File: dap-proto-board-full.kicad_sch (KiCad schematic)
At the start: 71 parts, among them J1 SFV18R-1STE1HLF, J2 UJ20-C-H-G-SMT-1-P16-TR, J3 SJ-3523-SMT, J4 JST_SH_SM03B-SRSS-TB, J6 Conn_01x06, J7 Conn_01x08, SW1 B3U-1000P, U1 TPD1E05U06DPY, U2 TAD5212, U3 TXS0108ERGYR, U4 W25Q64JWUUIQ, U5 TXS0108ERGYR, U6 MSD-11-A, U7 APS6404L-SQRH-ZR, U8 RP2350A, Y1 SIT8021AI-J4-XXS-12.288E, Y2 SIT8021AI-J4-XXS-11.289E, Y3 ABM8-272-T3

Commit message: I forgort what I did
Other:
- note added: "PIO_I2C"
- note removed: "I2C_1"
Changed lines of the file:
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@@
 		)
 	)
-	(text "I2C_1"
+	(text "PIO_I2C"
 		(exclude_from_sim no)
-		(at 345.694 133.604 0)
+		(at 347.218 133.604 0)
 		(effects
 			(font

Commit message: mostly finished; just need to breakout extra gpio
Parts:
- removed C10, C6, C7: 100nF, Capacitor_SMD:C_0402_1005Metric, symbol Device:C_Small
- removed C17: 1uF, Capacitor_SMD:C_0402_1005Metric, symbol Device:C
- removed C18, C26: 10nF, Capacitor_SMD:C_0402_1005Metric, symbol Device:C_Small
- removed C19, C20, C21, C22, C23, C24, C25, C27, C28, C29, C32, C34, C9: 100nF, Capacitor_SMD:C_0402_1005Metric, symbol Device:C
- removed C33: 4.7uF, Capacitor_SMD:C_0402_1005Metric, symbol Device:C
- removed C36: 2.2uF, Capacitor_SMD:C_0402_1005Metric, symbol Device:C_Small
- removed C5: 13pF, Capacitor_SMD:C_0402_1005Metric, symbol Device:C_Small
- removed J4: JST_SH_SM03B-SRSS-TB, Connector_JST:JST_SH_SM03B-SRSS-TB_1x03-1MP_P1.00mm_Horizontal, symbol Connector_Generic_MountingPin:Conn_01x03_MountingPin
- removed J6: Conn_01x06, Connector_PinSocket_2.54mm:PinSocket_1x06_P2.54mm_Vertical, symbol Connector_Generic:Conn_01x06
- removed J7: Conn_01x08, Connector_PinSocket_2.54mm:PinSocket_1x08_P2.54mm_Vertical, symbol Connector_Generic:Conn_01x08
- removed R1: 100k, Resistor_SMD:R_0402_1005Metric, symbol Device:R_Small
- removed R14: 4.7k, Resistor_SMD:R_0402_1005Metric, symbol Device:R_Small
- removed R15: 10, Resistor_SMD:R_0402_1005Metric, symbol Device:R_Small
- removed R3: 10k, Resistor_SMD:R_0402_1005Metric, symbol Device:R_Small
- removed R7: 1k, Resistor_SMD:R_0402_1005Metric, symbol Device:R
- removed R8, R9: 27, Resistor_SMD:R_0402_1005Metric, symbol Device:R
- removed U1: TPD1E05U06DPY, Package_SON:Texas_DPY0002A_0.6x1mm_P0.65mm, symbol Power_Protection:TPD1E05U06DPY
- removed U3, U5: TXS0108ERGYR, Package_DFN_QFN:Texas_RGY_R-PVQFN-N20_EP2.05x3.05mm_ThermalVias, symbol Logic_LevelTranslator:TXS0108EPW
- removed U4: W25Q64JWUUIQ, Package_SON:Winbond_USON-8-1EP_3x2mm_P0.5mm_EP0.2x1.6mm, symbol Memory_Flash:W25Q128JVS
- removed U7: APS6404L-SQRH-ZR, Package_SON:Winbond_USON-8-1EP_3x2mm_P0.5mm_EP0.2x1.6mm, symbol APS6404L-3SQR-ZR:APS6404L-3SQR-ZR
- removed U8: RP2350A, Package_DFN_QFN:QFN-60-1EP_7x7mm_P0.4mm_EP3.4x3.4mm, symbol MCU_RaspberryPi:RP2350A
- removed Y1: SIT8021AI-J4-XXS-12.288E, SIT8021AI-J4-XXS-24.000000E:OSC_SIT8021AI-J4-XXS-24.000000E, symbol SIT8021AI-J4-XXS-24.000000E:SIT8021AI-J4-XXS-24.000000E
- removed Y2: SIT8021AI-J4-XXS-11.289E, SIT8021AI-J4-XXS-24.000000E:OSC_SIT8021AI-J4-XXS-24.000000E, symbol SIT8021AI-J4-XXS-24.000000E:SIT8021AI-J4-XXS-24.000000E
- added C12, C15, C21, C23: 1uF, Capacitor_SMD:C_0603_1608Metric, symbol Device:C_Small
- added C13: 22uF, Capacitor_SMD:C_0603_1608Metric, symbol Device:C_Small
- added C14: 10nF, Capacitor_SMD:C_0603_1608Metric, symbol Device:C_Small
- added C16, C20, C22: 100nF, Capacitor_SMD:C_0603_1608Metric, symbol Device:C_Small
- added R13: 47k, Resistor_SMD:R_0603_1608Metric, symbol Device:R_Small
- added R7, R8, R9: 10k, Resistor_SMD:R_0603_1608Metric, symbol Device:R_Small
- added SW2: SW_Push, Button_Switch_SMD:SW_Push_1P1T_NO_Vertical_Wuerth_434133025816, symbol Switch:SW_Push
- added U2: USBLC6-2SC6, Package_TO_SOT_SMD:SOT-23-6, symbol Power_Protection:USBLC6-2SC6
- added U4: ESP32-S3, Package_DFN_QFN:QFN-56-1EP_7x7mm_P0.4mm_EP4x4mm_ThermalVias, symbol MCU_Espressif:ESP32-S3
- C1, C11, C2, C3, C4: footprint Capacitor_SMD:C_0402_1005Metric -> Capacitor_SMD:C_0603_1608Metric
- C10: renamed from C14; footprint Capacitor_SMD:C_0402_1005Metric -> Capacitor_SMD:C_0603_1608Metric
- C17: renamed from C30; value 15pF -> 18pF; footprint Capacitor_SMD:C_0402_1005Metric -> Capacitor_SMD:C_0603_1608Metric
- C18: renamed from C31; value 15pF -> 18pF; footprint Capacitor_SMD:C_0402_1005Metric -> Capacitor_SMD:C_0603_1608Metric
- C24: renamed from C35; footprint Capacitor_SMD:C_0402_1005Metric -> Capacitor_SMD:C_0603_1608Metric
- C5: renamed from C15; footprint Capacitor_SMD:C_0402_1005Metric -> Capacitor_SMD:C_0603_1608Metric
- C6: renamed from C16; footprint Capacitor_SMD:C_0402_1005Metric -> Capacitor_SMD:C_0603_1608Metric
- C7: renamed from C8; footprint Capacitor_SMD:C_0402_1005Metric -> Capacitor_SMD:C_0603_1608Metric
- C8: renamed from C12; footprint Capacitor_SMD:C_0402_1005Metric -> Capacitor_SMD:C_0603_1608Metric
- C9: renamed from C13; footprint Capacitor_SMD:C_0402_1005Metric -> Capacitor_SMD:C_0603_1608Metric
- R1: renamed from R13; value 1k -> 0; footprint Resistor_SMD:R_0402_1005Metric -> Resistor_SMD:R_0603_1608Metric
- R10, R11, R12: value 4.7k -> 47k; footprint Resistor_SMD:R_0402_1005Metric -> Resistor_SMD:R_0603_1608Metric
- R2: value 100k -> 10k; footprint Resistor_SMD:R_0402_1005Metric -> Resistor_SMD:R_0603_1608Metric
- R4: value 10k -> 2.2; footprint Resistor_SMD:R_0402_1005Metric -> Resistor_SMD:R_0603_1608Metric
- R5, R6: footprint Resistor_SMD:R_0402_1005Metric -> Resistor_SMD:R_0603_1608Metric
- SW1: value B3U-1000P -> SW_Push; footprint Button_Switch_SMD:SW_SPST_B3U-1000P -> Button_Switch_SMD:SW_Push_1P1T_NO_Vertical_Wuerth_434133025816; LCSC PN C231329 -> (none)
- U3: renamed from U2; footprint Package_DFN_QFN:TAD5212 -> footprints:VQFN24_RGE_CORNERPADS_TEX
- Y1: renamed from Y3; value ABM8-272-T3 -> ABM8-40.000MHZ-12-B1U-T
- renumbered H2 to H1, H1 to H2, U6 to U1
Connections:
- net 3v_SD_CS is gone; now on net SD_CS: U1.2 (CS)
- net 3v_SD_DAT1 is gone; now on net SD_DAT1: U1.8 (DAT1)
- net 3v_SD_DAT2 is gone; now on net SD_DAT2: U1.1 (DAT2)
- net 3v_SD_DIN is gone; now on net SD_DIN: U1.3 (DATA_IN)
- net 3v_SD_DOUT is gone; now on net SD_DOUT: U1.7 (DATA_OUT)
- net 3v_SD_SCLK is gone; now on net SD_SCLK: U1.5 (SCLK)
- net DISP_IO_ON is gone; now on net +3V3: R2.1
- net DIS_CLK1 is gone; now on net SD_DAT2: R5.2
- net DIS_CLK2 is gone; now on net SD_CS: R6.2
- net +3V3: now also C1.2, C2.1, C24.1, R10.1, R11.1, R12.1, R4.1, R5.1, R6.1, U3.6 (IOVDD), C12.1, C13.1, C14.1, C15.1, C16.1, C20.1, C21.1, C22.1, R13.1, R7.1, R8.1, R9.1, U4.2 (VDD3P3), U4.20 (VDD3P3_RTC), U4.29 (VDD_SPI), U4.3 (VDD3P3), U4.46 (VDD3P3_CPU), U4.55 (VDDA), U4.56 (VDDA)
- net BCLK: now also U4.12 (GPIO7)
- net DIN: now also U4.9 (GPIO4)
- net FSYNC: now also U4.11 (GPIO6)
- net GND: now also C12.2, C13.2, C14.2, C15.2, C16.2, C20.2, C21.2, C22.2, C23.2, SW2.2, U2.2 (GND), U4.57 (GND); no longer R2.2
- net GPIO9: now also U4.14 (GPIO9)
- net SD_CS: now also U4.47 (MTDI)
- net SD_DAT1: now also R9.2
- net SD_DIN: now also R7.2, U4.45 (MTDO)
- net SD_DOUT: now also R8.2, U4.43 (GPIO38)
- net SD_ON: now also U4.48 (MTMS)
- net SD_SCLK: now also U4.44 (MTCK)
- net USB_D+: now also U2.4 (I/O2), U4.26 (GPIO20/USB_D+); no longer J2.A6 (D+), J2.B6 (D+)
- net USB_D-: now also U2.6 (I/O1), U4.25 (GPIO19/USB_D-); no longer J2.A7 (D-), J2.B7 (D-)
- net VBUS: now also U2.5 (VBUS)
- net XIN: now also R1.1, U4.53 (XTAL_N); no longer C17.1, Y1.1
- net XOUT: now also C17.1, Y1.1, U4.54 (XTAL_P); no longer R1.1
- net disp_LITE: now also U4.27 (GPIO21)
- net disp_MISO: now also U4.40 (GPIO35)
- net disp_MOSI: now also U4.39 (GPIO34)
- net npm_SCL: now also R10.2, U4.15 (GPIO10); no longer R11.2
- net npm_SDA: now also R11.2, U4.16 (GPIO11); no longer R10.2
- net tad_SCL: now also R13.2, U4.7 (GPIO2)
- net tad_SDA: now also U4.6 (GPIO1)
- net tad_GPO1: now reaches U3.11 (GPO1)
- net DOUT: now reaches U3.4 (DOUT)
- net DOUT: now also U4.10 (GPIO5)
- removed net +1V8: C1.2, C10.2, C2.1, C24.1, C9.2, R10.1, R11.1, R12.1, R4.1, R5.1, R6.1, U3.23 (AVDD), U3.6 (IOVDD)
- net PSRAM_CS: no longer names the net of R4.2
- net PSRAM_CS: now also C10.2, C9.2, U3.23 (AVDD)
- net disp_CS_SCL renamed disp_CS
- net disp_CS: now also U4.42 (GPIO37); no longer J1.13 (Pin_13)
- net disp_DC_SDA renamed disp_DC
- net disp_DC: now also U4.41 (GPIO36); no longer J1.14 (Pin_14)
- net disp_SCK renamed disp_SCLK
- net disp_SCLK: now also U4.38 (GPIO33)
- net ~{USB_BOOT}: no longer names the net of SW1.2
- net ~{USB_BOOT}: now also U4.5 (GPIO0)
- new net: C23.1, R2.2, SW2.1, U4.4 (CHIP_PU)
- new net: J2.A6 (D+), J2.B6 (D+), U2.3 (I/O2)
- new net: J2.A7 (D-), J2.B7 (D-), U2.1 (I/O1)
- new net GPIO13: U4.18 (GPIO13)
- new net GPIO14: U4.19 (GPIO14)
- new net GPIO15: U4.21 (XTAL_32K_P)
- new net GPIO16: U4.22 (XTAL_32K_N)
- new net GPIO17: U4.23 (GPIO17)
- new net GPIO18: U4.24 (GPIO18)
- new net GPIO43: U4.49 (U0TXD)
- new net GPIO44: U4.50 (U0RXD)
- new net GPIO45: U4.51 (GPIO45)
- new net GPIO46: U4.52 (GPIO46)
- new net GPIO8: U4.13 (GPIO8)
- new net disp_SCL: J1.13 (Pin_13)
- new net disp_SDA: J1.14 (Pin_14)
- new net npm_GPIO1: U4.17 (GPIO12)
- no-connect marks 25 -> 24
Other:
- note added: "40MHz Crystal"
- note removed: "1.8v -> 3.3v Display logic level shifter"
- note removed: "1.8v -> 3.3v SD logic level shifter"
- note removed: "12MHz Crystal"
- note removed: "Default standby"
- note removed: "Extra GPIO"
- note removed: "Flash"
- note removed: "Has internal pull ups to ensure data lines are well-defined"
- note removed: "I2C_0"
- note removed: "JST Debug Connector"
- note removed: "Make sure these resistors are close to MCU"
- note removed: "PIO_I2C"
- note removed: "PSRAM"
- note removed: "RP2350A"
- note removed: "VREG filter"
- note removed: "from load switch"
- moved on the sheet: C17, C18, C5, C6, H1, H2, J3, R1, U1, Y1

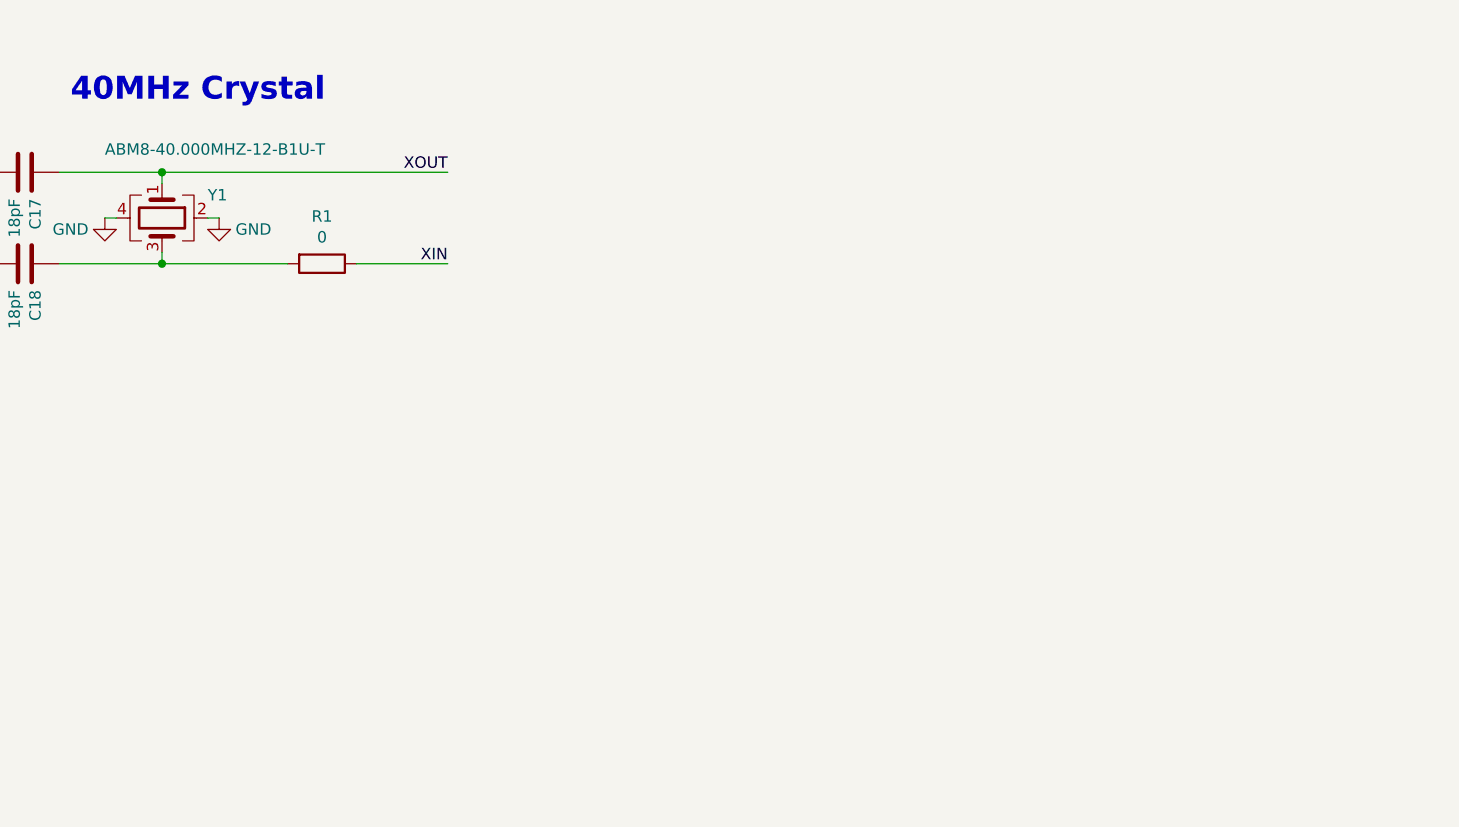
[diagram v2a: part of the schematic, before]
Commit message: breakout extra gpios; gen gerbers and images
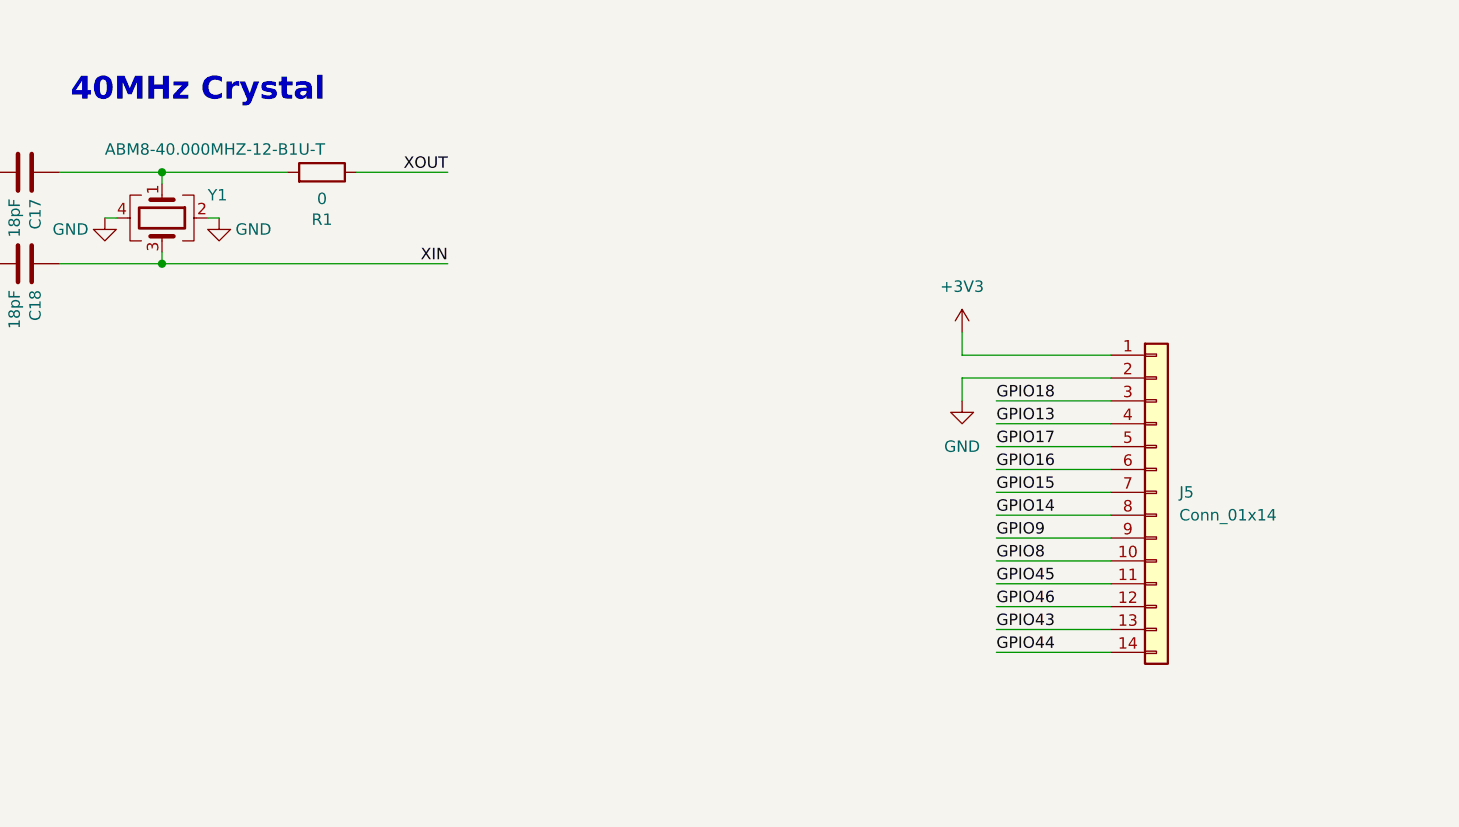
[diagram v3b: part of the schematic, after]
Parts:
- added J5: Conn_01x14, Connector_PinSocket_2.54mm:PinSocket_1x14_P2.54mm_Vertical, symbol Connector_Generic:Conn_01x14
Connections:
- net +3V3: now also J5.1 (Pin_1)
- net GND: now also J5.2 (Pin_2)
- net GPIO13: now also J5.4 (Pin_4)
- net GPIO14: now also J5.8 (Pin_8)
- net GPIO15: now also J5.7 (Pin_7)
- net GPIO16: now also J5.6 (Pin_6)
- net GPIO17: now also J5.5 (Pin_5)
- net GPIO18: now also J5.3 (Pin_3)
- net GPIO43: now also J5.13 (Pin_13)
- net GPIO44: now also J5.14 (Pin_14)
- net GPIO45: now also J5.11 (Pin_11)
- net GPIO46: now also J5.12 (Pin_12)
- net GPIO8: now also J5.10 (Pin_10)
- net GPIO9: now also J5.9 (Pin_9)
- net XIN: now also C18.1, Y1.3; no longer R1.1
- net XOUT: now also R1.1; no longer C17.1, Y1.1
- new net: C17.1, R1.2, Y1.1
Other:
- moved on the sheet: R1
